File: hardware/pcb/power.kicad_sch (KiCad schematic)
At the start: 75 parts, among them J1 XT30PW-F, J12 Solar, J13 USB-C, Q3 AO3407, Q4 BSS123, Q5 AO3407, U1 AP63203WU, U11 USBLC6, U12 IP2326, U7 CN3722, U8 MT3608B

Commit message: hw(pcb): apply approved swaps — AO3400A, SI2319CDS, HRO USB-C, DNF GDT footprints
All four user-approved swaps from the better-options review:
- Q2/Q4 BSS123 -> AO3400A (Vgs(th) max 1.45 V at 3.3 V drive; LCSC
  C20917, 2N7002 second source)
- M_SOLAR AO3407 -> SI2319CDS (-40 V, >60% Vds margin restored; new
  welld:SI2319CDS lib symbol with identical pin geometry; Vishay
  C146287, VBsemi alternate C558254). D5/Q3/Q5 stay AO3407.
- J13 GCT USB4135 -> HRO TYPE-C-31-M-12 (C165948); footprint name
  flagged for verification against the installed KiCad lib; B-side
  mirror-pad net check noted for layout.
- GDT1/GDT2 (DNF, 90 V 2-pole) added on LOOP_TERM_CH1/CH2 to GND —
  completes the industrial GDT->R->TVS surge chain for field wiring;
  populate per site. WellD.pretty land pattern flagged for layout.

netlist_check: 397 pins / 78 nets / 20 NC / zero mismatches; all five
sheets balance. Case note: re-check the USB-C cutout for the HRO shell
once layout places J13. No GPIO or firmware changes.

Co-Authored-By: Claude Fable 5 <noreply@anthropic.com>
Claude-Session: https://claude.ai/code/session_01VtMFY5Q94iYbsNPpLcPJyK
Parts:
- J13: footprint Connector_USB:USB_C_Receptacle_GCT_USB4135-GF-A_6P_TopMnt_Horizontal -> Connector_USB:USB_C_Receptacle_HRO_TYPE-C-31-M-12
- M_SOLAR: value AO3407 -> SI2319CDS; symbol welld:AO3407 -> welld:SI2319CDS; LCSC C31417 -> C146287
- Q4: value BSS123 -> AO3400A
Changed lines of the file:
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@@
 			)
 		)
-		(property "Footprint" "Connector_USB:USB_C_Receptacle_GCT_USB4135-GF-A_6P_TopMnt_Horizontal"
+		(property "Footprint" "Connector_USB:USB_C_Receptacle_HRO_TYPE-C-31-M-12"
 			(at 0 0 0)
 			(hide yes)
@@
 	)
 	(symbol
-		(lib_id "welld:AO3407")
+		(lib_id "welld:SI2319CDS")
 		(at 137.16 127 0)
 		(unit 1)
@@
 			)
 		)
-		(property "Value" "AO3407"
+		(property "Value" "SI2319CDS"
 			(at 137.16 129 0)
 			(show_name no)
@@
 			)
 		)
-		(property "LCSC" "C31417"
+		(property "LCSC" "C146287"
 			(at 0 0 0)
 			(hide yes)
@@
 			)
 		)
-		(property "Value" "BSS123"
+		(property "Value" "AO3400A"
 			(at 198.12 143.24 0)
 			(show_name no)
@@
 	(wire
 		(pts
-			(xy 57.15 91.44) (xy 59.69 91.44)
-		)
-		(stroke
-			(width 0)
-			(type default)
-		)
-	)
-	(label "AP_BST"
-		(at 57.15 91.44 0)
-		(effects
-			(font
-				(size 1.27 1.27)
-			)
-			(justify left bottom)
-		)
-	)
-	(wire
-		(pts
-			(xy 45.72 91.44) (xy 48.26 91.44)
-		)
-		(stroke
-			(width 0)
-			(type default)
-		)
-	)
-	(label "AP_BST"
-		(at 48.26 91.44 0)
-		(effects
-			(font
-				(size 1.27 1.27)
-			)
-			(justify left bottom)
-		)
-	)
-	(wire
-		(pts
-			(xy 45.72 99.06) (xy 48.26 99.06)
-		)
-		(stroke
-			(width 0)
-			(type default)
-		)
-	)
-	(label "AP_SW"
-		(at 48.26 99.06 0)
-		(effects
-			(font
-				(size 1.27 1.27)
-			)
-			(justify left bottom)
-		)
-	)
-	(wire
-		(pts
 			(xy 72.39 91.44) (xy 74.93 91.44)
 		)
@@
 	(wire
 		(pts
+			(xy 59.69 91.44) (xy 57.15 91.44)
+		)
+		(stroke
+			(width 0)
+			(type default)
+		)
+	)
+	(label "AP_BST"
+		(at 57.15 91.44 180)
+		(effects
+			(font
+				(size 1.27 1.27)
+			)
+			(justify right bottom)
+		)
+	)
+	(wire
+		(pts
+			(xy 45.72 91.44) (xy 45.72 88.9)
+		)
+		(stroke
+			(width 0)
+			(type default)
+		)
+	)
+	(label "AP_BST"
+		(at 45.72 88.9 90)
+		(effects
+			(font
+				(size 1.27 1.27)
+			)
+			(justify left bottom)
+		)
+	)
+	(wire
+		(pts
 			(xy 90 93.98) (xy 90 96.52)
 		)
@@
 	(wire
 		(pts
+			(xy 45.72 99.06) (xy 45.72 101.6)
+		)
+		(stroke
+			(width 0)
+			(type default)
+		)
+	)
+	(label "AP_SW"
+		(at 45.72 101.6 270)
+		(effects
+			(font
+				(size 1.27 1.27)
+			)
+			(justify right bottom)
+		)
+	)
+	(wire
+		(pts
 			(xy 156.21 22.86) (xy 158.75 22.86)
 		)
@@
 	)
 	(no_connect
-		(at 173.99 22.86)
+		(at 161.29 25.4)
 	)
 	(no_connect
-		(at 161.29 25.4)
+		(at 173.99 22.86)
 	)
 	(no_connect

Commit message: hw(pcb): convert power architecture to 1S — TP4056 + CN3791 + HT7333-A
Pack 2S1P -> 1S2P (VBAT 3.0-4.2 V; user decision, chosen over 2S for
simplicity/ecosystem). IP2326 boost subsystem deleted -> TP4056 1 A linear
USB charger; CN3722 + external buck stage deleted -> CN3791 integrated-switch
1S MPPT charger (/CHRG_SOLAR net and GPIO map unchanged); AP63203WU buck
(VIN min 3.8 V) deleted -> HT7333-A LDO. D13 -> SMAJ5.0A, D8/D14 -> SMAJ10CA,
R7 330k -> 100k (/2 divider), F2 footprint 1206 -> 1812 per blocker 8.
Netlist re-verified: 337 pins / 63 nets / 10 NC / zero mismatches.
Docs updated: schematic_connections (new 1S blockers 10a-e), BOM, placement
groups B/D/G/L, fab checklist, component-review addendum, CHANGELOG.

Co-Authored-By: Claude Fable 5 <noreply@anthropic.com>
Claude-Session: https://claude.ai/code/session_01VtMFY5Q94iYbsNPpLcPJyK
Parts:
- removed C_BST2, C_BST_AP, C_COM3: 100nF, Capacitor_SMD:C_0402_1005Metric, symbol Device:C
- removed C_COM1: 470pF, Capacitor_SMD:C_0402_1005Metric, symbol Device:C
- removed C_COM2: 220nF, Capacitor_SMD:C_0402_1005Metric, symbol Device:C
- removed C_SYS1, C_SYS2: 22uF 25V, Capacitor_SMD:C_1206_3216Metric, symbol Device:C
- removed D16: SS34, Diode_SMD:D_SMA, symbol Device:D_Schottky
- removed L2: 4.7uH, Inductor_SMD:L_Vishay_IFSC-1515AH_4x4x1.8mm, symbol Device:L
- removed L3: 2.2uH, Inductor_SMD:L_Bourns-SRN6045TA, symbol Device:L
- removed M_SOLAR: SI2319CDS, Package_TO_SOT_SMD:SOT-23, symbol welld:SI2319CDS
- removed R11: 10k, Resistor_SMD:R_0402_1005Metric, symbol Device:R
- removed R33: 243k, Resistor_SMD:R_0402_1005Metric, symbol Device:R
- removed R34: 100k, Resistor_SMD:R_0402_1005Metric, symbol Device:R
- removed R35: 90k, Resistor_SMD:R_0402_1005Metric, symbol Device:R
- removed R_COM2: 120R, Resistor_SMD:R_0402_1005Metric, symbol Device:R
- removed R_FBH: 560k, Resistor_SMD:R_0402_1005Metric, symbol Device:R
- removed R_FBL: 124k, Resistor_SMD:R_0402_1005Metric, symbol Device:R
- removed R_VSET: 120k, Resistor_SMD:R_0603_1608Metric, symbol Device:R
- removed U1: AP63203WU, Package_TO_SOT_SMD:TSOT-23-6, symbol welld:AP63203WU
- removed U12: IP2326, Package_DFN_QFN:QFN-24-1EP_4x4mm_P0.5mm_EP2.6x2.6mm, symbol welld:IP2326
- removed U7: CN3722, Package_SO:TSSOP-16_4.4x5mm_P0.65mm, symbol welld:CN3722
- added R_NTC: 5k6, Resistor_SMD:R_0402_1005Metric, symbol Device:R
- added R_PROG: 1k2, Resistor_SMD:R_0402_1005Metric, symbol Device:R
- added U1: HT7333-A, Package_TO_SOT_SMD:SOT-23, symbol welld:HT7333
- added U12: TP4056, Package_SO:SOIC-8-1EP_3.9x4.9mm_P1.27mm_EP2.29x2.29mm, symbol welld:TP4056
- added U7: CN3791, Package_SO:SSOP-10_3.9x4.9mm_P1.00mm, symbol welld:CN3791
- D13: value SMAJ10CA -> SMAJ5.0A
- D14, D8: value SMAJ24CA -> SMAJ10CA
- F2: footprint Fuse:Fuse_1206_3216Metric -> Fuse:Fuse_1812_4532Metric
- R19: value 0R4 -> 0R1
- R20: value 158k -> 316k
- R21: value 10k -> 100k
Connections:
- net SOLAR_FW is gone; now on net SOLAR_SW: D_SOLAR.1 (K), L_SOLAR.1
- net +3V3: now also U1.2 (VOUT)
- net /CHRG_SOLAR: now also U7.4 (/CHRG)
- net /CHRG_USB: now also U12.7 (/CHRG)
- net CN_CS: now also U7.9 (CSP)
- net CN_VG: now also U7.8 (VG)
- net GND: now also R_PROG.2, U1.1 (GND), U12.3 (GND), U12.9 (EPAD), U7.2 (GND)
- net MPPT_REF: now also U7.1 (MPPT)
- net SOLAR_SW: now also U7.7 (SW)
- net TEMP_SOLAR: now also U7.5 (TEMP)
- net USB_NTC: now also R_NTC.2, U12.1 (TEMP)
- net VBAT: now also U1.3 (VIN), U12.5 (BAT), U7.10 (BAT)
- net VSOLAR: now also U7.6 (VCC)
- net VUSB: now also R_NTC.1, U12.4 (VCC), U12.8 (CE)
- new net USB_PROG: R_PROG.1, U12.2 (PROG)
- no-connect marks 14 -> 4

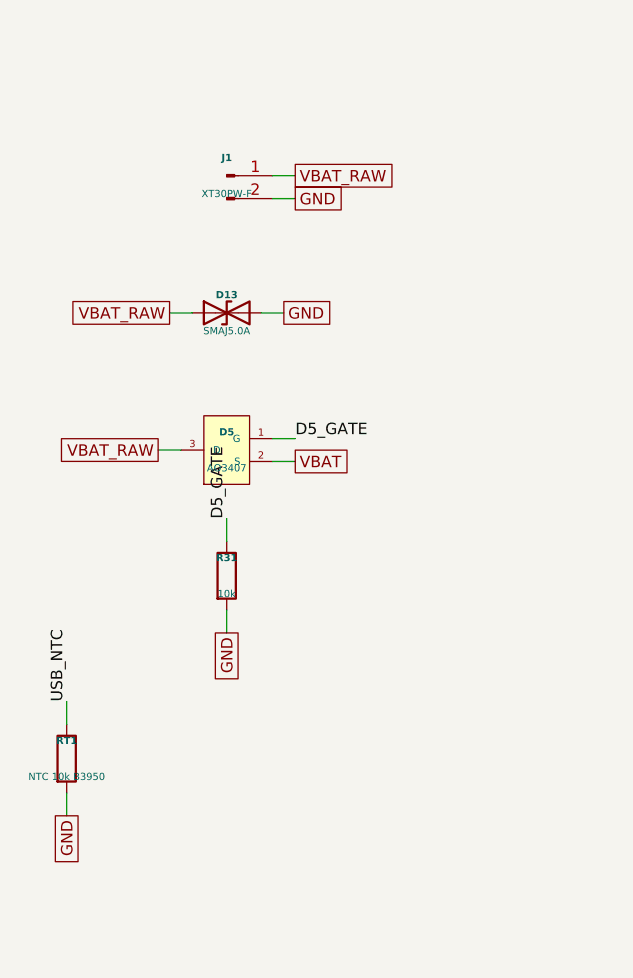
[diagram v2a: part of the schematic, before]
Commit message: hw(pcb): generic 18650 in on-board carrier + DW01A/FS8205A protection
Replace the Sinowatt pack + XT30 (J1) with a single generic 18650 in a
THT carrier (BT1). Generic bare cells have no PCM, so the standard 1S
protection pair is added in the cell- path: DW01A supervisor + FS8205A
dual N-FET (100R/100n VCC filter, 1k CS — the TP4056-ecosystem reference
topology; pinouts flagged for datasheet confirmation as blocker #11).
D5 now guards reversed cell insertion; D13 stays at the cell+ tab.
Netlist: 357 pins / 69 nets / 11 NC / zero mismatches.
Docs: net reference (+design change #19, blockers #11a-c, #7a retired),
BOM, placement Group H (carrier dominates the 80x55 outline — back-side
or grow, layout call), fab checklist, README, agent defs; '1S2P pack'
references swept. PROJECT_VER 1.1.0 -> 1.1.1 (Kconfig help text).

Co-Authored-By: Claude Fable 5 <noreply@anthropic.com>
Claude-Session: https://claude.ai/code/session_01VtMFY5Q94iYbsNPpLcPJyK
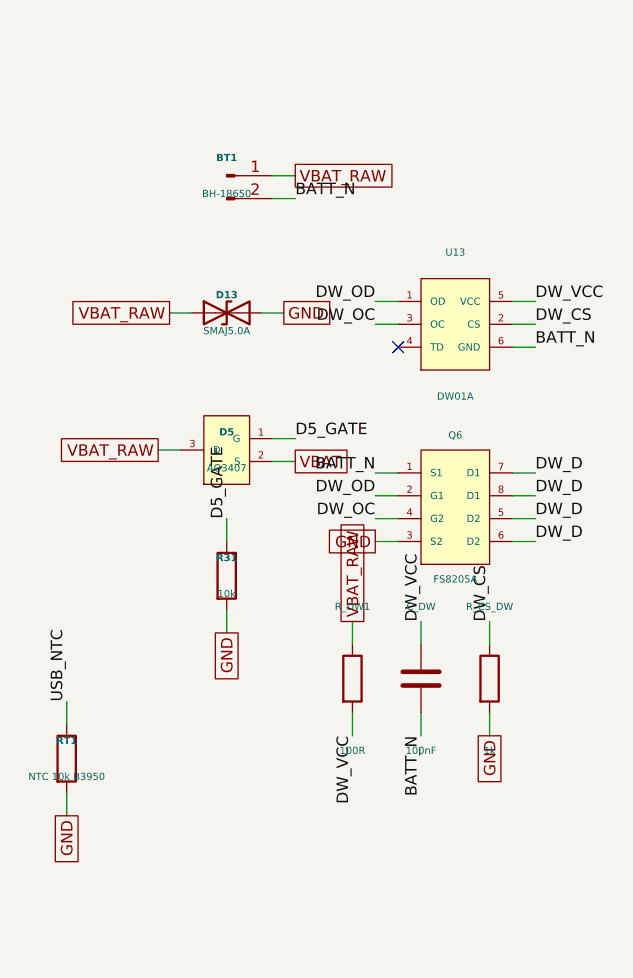
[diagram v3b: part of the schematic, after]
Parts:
- added C_DW: 100nF, Capacitor_SMD:C_0402_1005Metric, symbol Device:C
- added Q6: FS8205A, Package_SO:TSSOP-8_4.4x3mm_P0.65mm, symbol welld:FS8205A
- added R_CS_DW: 1k, Resistor_SMD:R_0402_1005Metric, symbol Device:R
- added R_DW1: 100R, Resistor_SMD:R_0402_1005Metric, symbol Device:R
- added U13: DW01A, Package_TO_SOT_SMD:SOT-23-6, symbol welld:DW01A
- BT1: renamed from J1; value XT30PW-F -> BH-18650; footprint WellD:XT30PW-F_RightAngle -> WellD:BH-18650_THT
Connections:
- net GND: now also Q6.3 (S2), R_CS_DW.2; no longer BT1.2 (Pin_2)
- net VBAT_RAW: now also R_DW1.1
- new net BATT_N: BT1.2 (Pin_2), C_DW.2, Q6.1 (S1), U13.6 (GND)
- new net DW_CS: R_CS_DW.1, U13.2 (CS)
- new net DW_D: Q6.5 (D2), Q6.6 (D2), Q6.7 (D1), Q6.8 (D1)
- new net DW_OC: Q6.4 (G2), U13.3 (OC)
- new net DW_OD: Q6.2 (G1), U13.1 (OD)
- new net DW_VCC: C_DW.1, R_DW1.2, U13.5 (VCC)
- no-connect marks 4 -> 5

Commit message: hw(pcb): datasheet-verification pass — CN3791 controller correction + verified pinouts
Verified all five 1S-conversion parts against web datasheet sources and
the Soldered Electronics open-hardware CN3791 KiCad design:
- TP4056 (C16581 ESOP-8), HT7333-A (C21583), DW01A: confirmed as drawn.
- CN3791: CORRECTED — it is an external-P-FET controller (pin map
  VG=1..DRV=10, no TEMP pin). Restored M_SOLAR (SI2319CDS) + D16 + R_DRV,
  added COM network (220nF+120R), deleted RT_SOLAR. I_CH=120mV/Rcs
  verified (0.1R -> 1.2A); VG cap to VCC verified; BAT+CSP sleep 9uA.
- FS8205A: CORRECTED — real TSSOP-8 map D=1&8, S1=2&3, G1=4, G2=5,
  S2=6&7 (drains internally common); symbol redrawn and rewired.
- Carrier MPNs picked: MY-18650-02 THT clip pair (C2979182, recommended)
  or BH-18650-B1BA002 (C2988620); footprint drawn from LCSC drawing at
  order time.
NEW decision item #10f: solar path has no cold-charge cutoff (CN3791
lacks a TEMP pin) — decide before winter deployment.
Netlist: 366 pins / 72 nets / 11 NC / zero mismatches.

Co-Authored-By: Claude Fable 5 <noreply@anthropic.com>
Claude-Session: https://claude.ai/code/session_01VtMFY5Q94iYbsNPpLcPJyK
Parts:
- removed RT_SOLAR: NTC 10k B3950, Resistor_SMD:R_0603_1608Metric, symbol Device:R
- added C_COM: 220nF, Capacitor_SMD:C_0402_1005Metric, symbol Device:C
- added D16: SS34, Diode_SMD:D_SMA, symbol Device:D_Schottky
- added M_SOLAR: SI2319CDS, Package_TO_SOT_SMD:SOT-23, symbol welld:SI2319CDS
- added R_COM: 120R, Resistor_SMD:R_0402_1005Metric, symbol Device:R
- added R_DRV: 300k, Resistor_SMD:R_0402_1005Metric, symbol Device:R
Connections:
- net /CHRG_SOLAR: now also U7.3 (/CHRG); no longer U7.4 (/CHRG)
- net BATT_N: now also Q6.2 (S1), Q6.3 (S1); no longer Q6.1 (S1)
- net CN_CS: now also U7.8 (CSP); no longer U7.9 (CSP)
- net CN_VG: now also U7.1 (VG); no longer U7.8 (VG)
- net DW_D: now also Q6.1 (D); no longer Q6.5 (D2), Q6.6 (D2), Q6.7 (D1)
- net DW_OC: now also Q6.5 (G2); no longer Q6.4 (G2)
- net DW_OD: now also Q6.4 (G1); no longer Q6.2 (G1)
- net GND: now also Q6.6 (S2), Q6.7 (S2), R_COM.2; no longer Q6.3 (S2)
- net MPPT_REF: now also U7.6 (MPPT); no longer U7.1 (MPPT)
- net SOLAR_SW: now also D16.2 (A), M_SOLAR.3 (D); no longer D_SOLAR.1 (K), L_SOLAR.1, U7.7 (SW)
- net VBAT: now also U7.7 (BAT); no longer U7.10 (BAT)
- net VSOLAR: now also U7.9 (VCC), M_SOLAR.2 (S), R_DRV.1; no longer U7.6 (VCC)
- net TEMP_SOLAR renamed CN_COM
- net CN_COM: now also C_COM.1
- new net CN_DRV: M_SOLAR.1 (G), R_DRV.2, U7.10 (DRV)
- new net COM_RC: C_COM.2, R_COM.1
- new net SOLAR_FW: D16.1 (K), D_SOLAR.1 (K), L_SOLAR.1

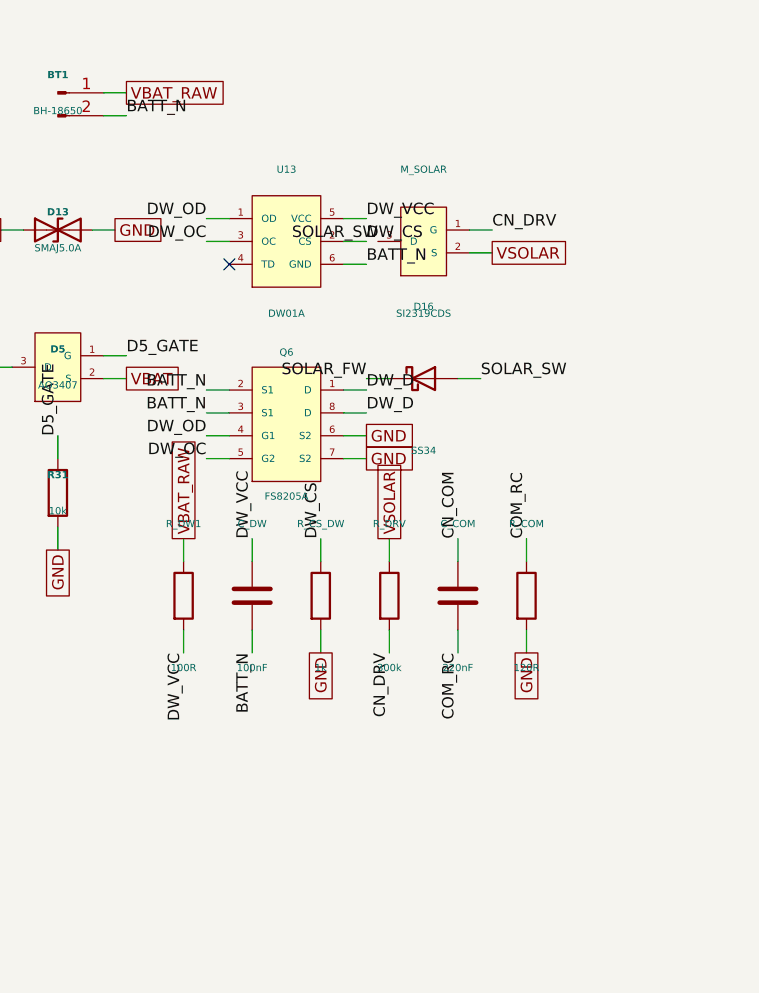
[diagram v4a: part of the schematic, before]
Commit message: hw(pcb): add solar cold-charge cutoff — LM393 MPPT clamp, zero night draw
User decision (resolves #10f): the CN3791 has no TEMP pin, so cold-charge
protection is discrete. LM393 (U14) powered from VSOLAR — dead panel means
dead circuit, zero battery draw at night; both dividers ratiometric to
VSOLAR so the threshold is panel-voltage independent. RT_SOLAR revived
(10k B3950, coupled to the cell) against R_NT1 30k -> trip ~+2C falling;
R_HYS 330k -> release ~+4C. OUT1 drives Q7 (AO3400A) which clamps the
CN3791 MPPT pin below its 1.205V reference — the controller backs duty
to zero exactly as with a collapsed panel. Unused comparator half parked;
OUT2 NC. Netlist: 391 pins / 75 nets / 12 NC / zero mismatches.

Co-Authored-By: Claude Fable 5 <noreply@anthropic.com>
Claude-Session: https://claude.ai/code/session_01VtMFY5Q94iYbsNPpLcPJyK
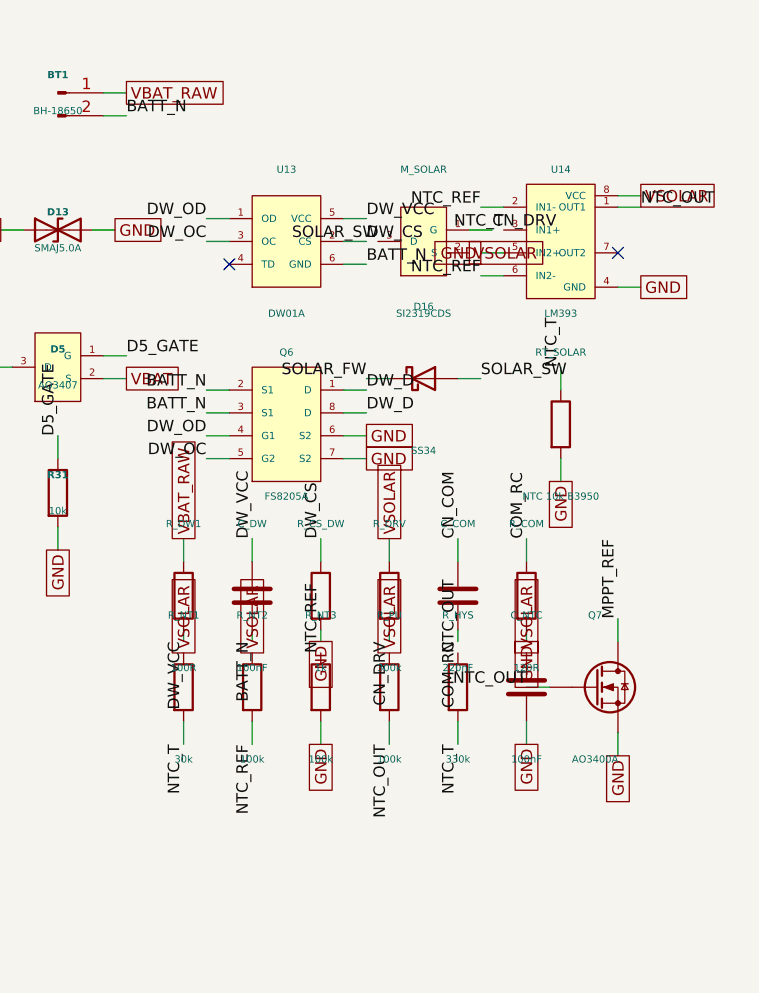
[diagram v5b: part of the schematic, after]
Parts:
- added C_NTC: 100nF, Capacitor_SMD:C_0402_1005Metric, symbol Device:C
- added Q7: AO3400A, Package_TO_SOT_SMD:SOT-23, symbol Device:Q_NMOS
- added RT_SOLAR: NTC 10k B3950, Resistor_SMD:R_0603_1608Metric, symbol Device:R
- added R_HYS: 330k, Resistor_SMD:R_0402_1005Metric, symbol Device:R
- added R_NT1: 30k, Resistor_SMD:R_0402_1005Metric, symbol Device:R
- added R_NT2, R_NT3, R_PU: 100k, Resistor_SMD:R_0402_1005Metric, symbol Device:R
- added U14: LM393, Package_SO:SOIC-8_3.9x4.9mm_P1.27mm, symbol welld:LM393
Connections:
- net GND: now also C_NTC.2, Q7.S, RT_SOLAR.2, R_NT3.2, U14.4 (GND), U14.5 (IN2+)
- net MPPT_REF: now also Q7.D
- net VSOLAR: now also C_NTC.1, R_NT1.1, R_NT2.1, R_PU.1, U14.8 (VCC)
- new net NTC_OUT: Q7.G, R_HYS.1, R_PU.2, U14.1 (OUT1)
- new net NTC_REF: R_NT2.2, R_NT3.1, U14.2 (IN1-), U14.6 (IN2-)
- new net NTC_T: RT_SOLAR.1, R_HYS.2, R_NT1.2, U14.3 (IN1+)
- no-connect marks 5 -> 6

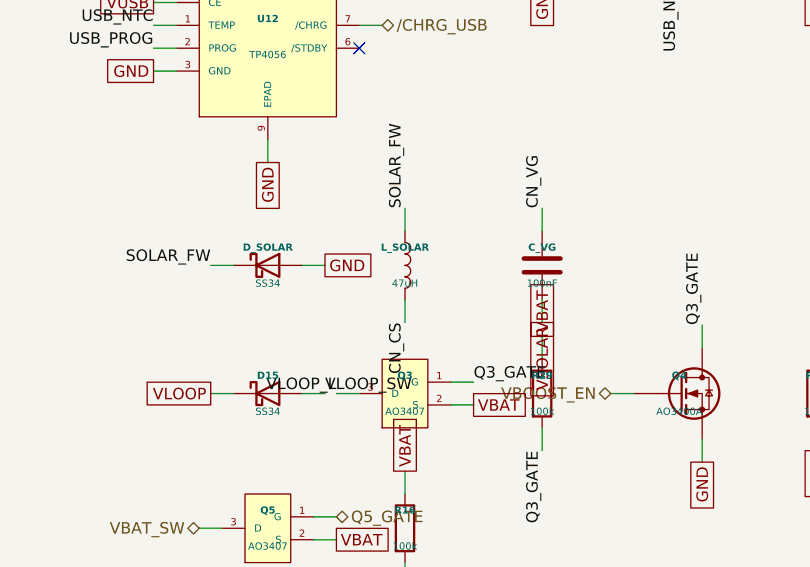
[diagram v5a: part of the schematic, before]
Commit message: hw(pcb): compute TP4056 NTC window + resize L_SOLAR (bench-math resolved)
Worked the two remaining 'assumed/bench' items into computed results:

TP4056 cold-charge window (R_NTC 5.6k / RT1 10k B3950): computed +8..+44 C
(cold trip RT1=22.4k at 80%%.VIN -> +7.9 C; hot trip RT1=4.58k at 45%%.VIN
-> +43.7 C). The doc's earlier '+5..+44' was optimistic on the cold end;
+8 C is conservative-safe for Li-ion (below ~+5 C risks plating), so 5.6k
is kept. Noted the 6.8k option (+4..+39 C) for reference.

L_SOLAR: computed peak inductor current ~1.24 A (Ich 1.2 A + half of 85 mA
ripple at 47 uH). The old SRN6045TA-470M (Isat 1.3 A) gave only ~5%% margin.
Changed to SRN6045TA-220M (22 uH, Isat 3.3 A, Irms 2.3 A, DCR 96 mOhm) —
same 6045 footprint, no redraw, 1.7x margin over the 1.9 A target; ripple
rises to 182 mApp, still trivial. Schematic value 47uH->22uH.

Netlist unchanged: 391 pins / 75 nets / 12 NC / zero mismatches.

Co-Authored-By: Claude Opus 4.8 <noreply@anthropic.com>
Claude-Session: https://claude.ai/code/session_01VtMFY5Q94iYbsNPpLcPJyK
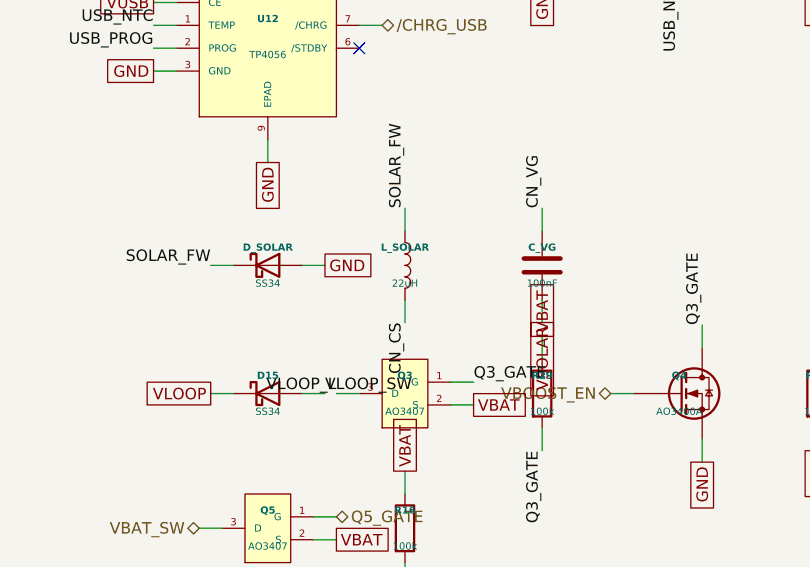
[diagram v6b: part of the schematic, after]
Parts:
- L_SOLAR: value 47uH -> 22uH
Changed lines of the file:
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@@
 			)
 		)
-		(property "Value" "47uH"
+		(property "Value" "22uH"
 			(at 167.64 129 0)
 			(show_name no)
